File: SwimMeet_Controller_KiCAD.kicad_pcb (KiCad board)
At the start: 2 copper layers, 152.4 x 76.2 mm, 38 parts, among them SW1 LEFT, SW10 RIGHT, SW11 UP, SW12 DOWN, SW13 ACCEPT, SW2 NEXT_HEAT, SW3 PREV_EVENT, SW4 NEXT_EVENT, SW5 PREV_HEAT, SW6 GET_TIMES, SW7 SCORE_EVENT, SW8 CLOSE, SW9 ENTER, U1 Digispark_USB-A_16.5MHz, U2 MCP23017-E_SO

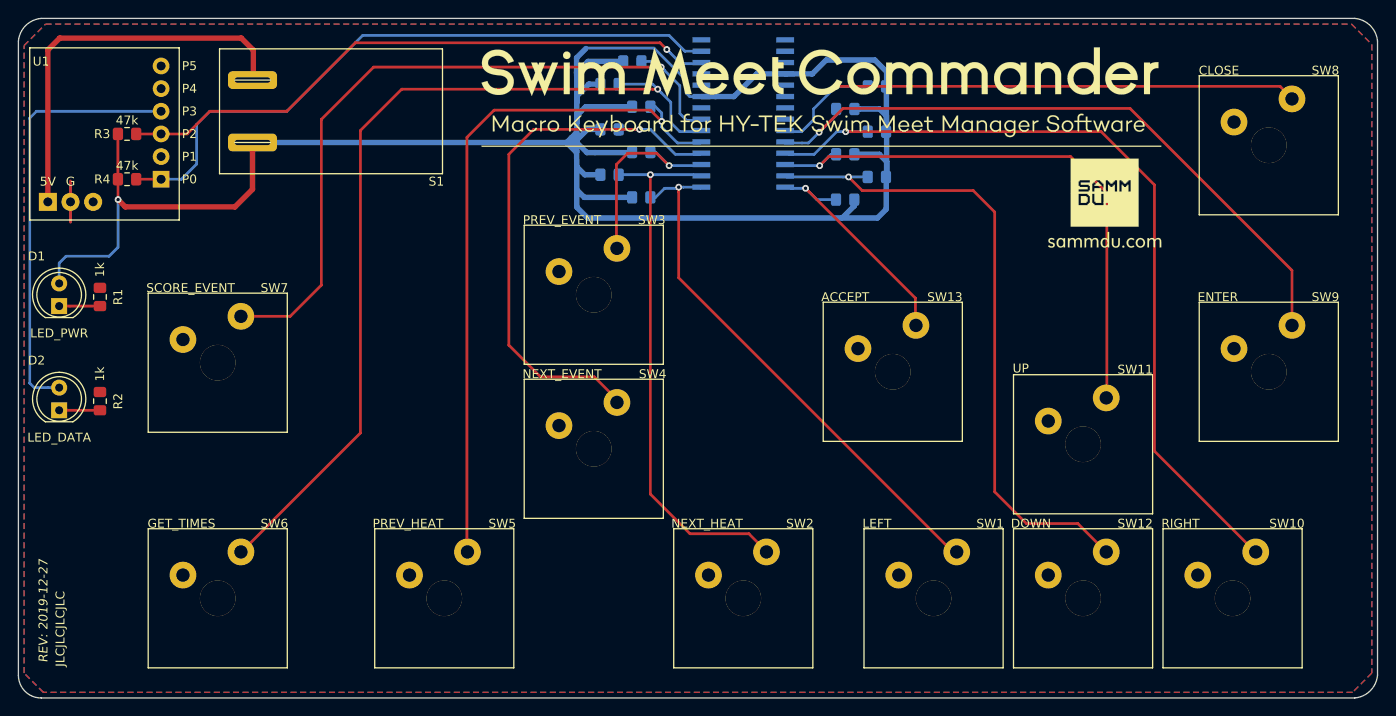
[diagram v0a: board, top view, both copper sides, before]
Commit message: used proper power symbols in schem; made schem compatible with larger grid size; added net names; tidy'ed up PCB more
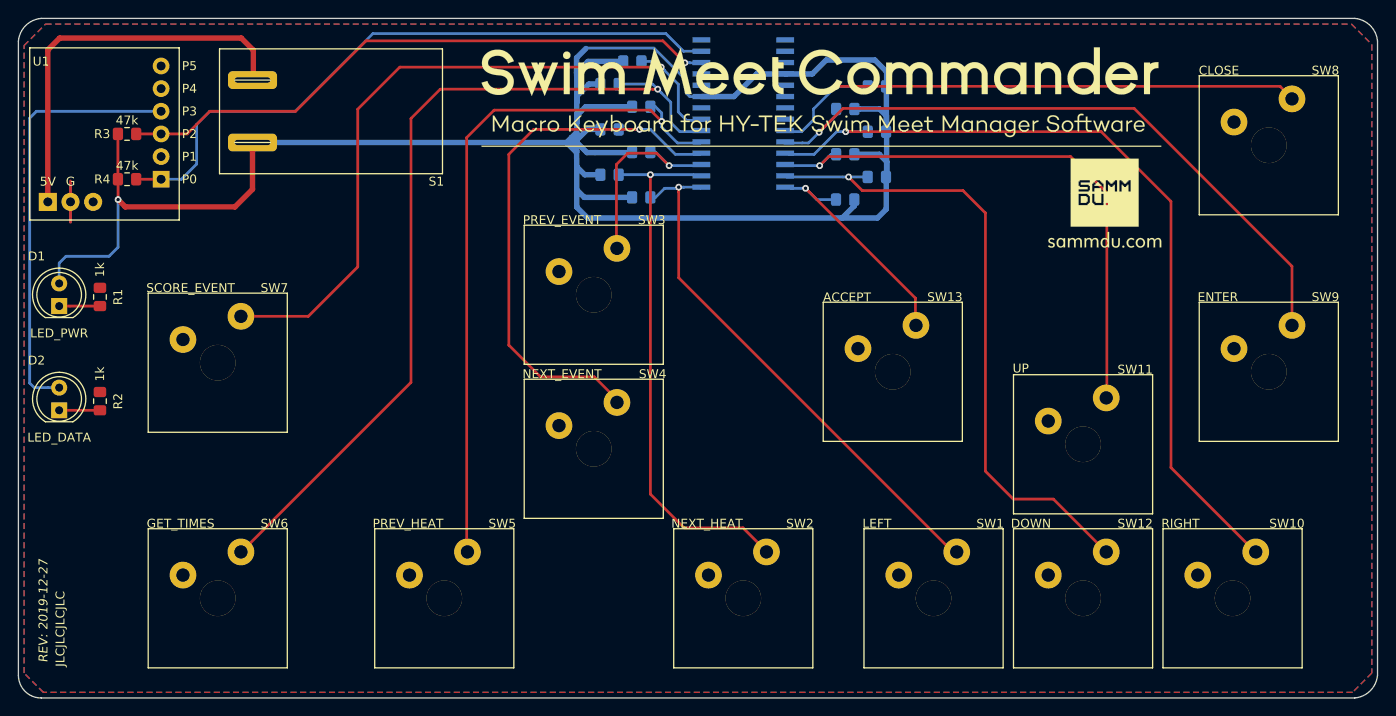
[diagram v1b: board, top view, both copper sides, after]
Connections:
- net 5V renamed +5V
- net Net-(D2-Pad2) renamed /SIG_DATA
- net Net-(S1-Pad2) renamed /VREG
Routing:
- net Net-(R10-Pad2): track 101.2 -> 98.6 mm
- net Net-(R16-Pad2): track 73.8 -> 72.4 mm
- net Net-(R11-Pad2): track 81.3 -> 80.8 mm

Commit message: implemented polygons for 5V+ net
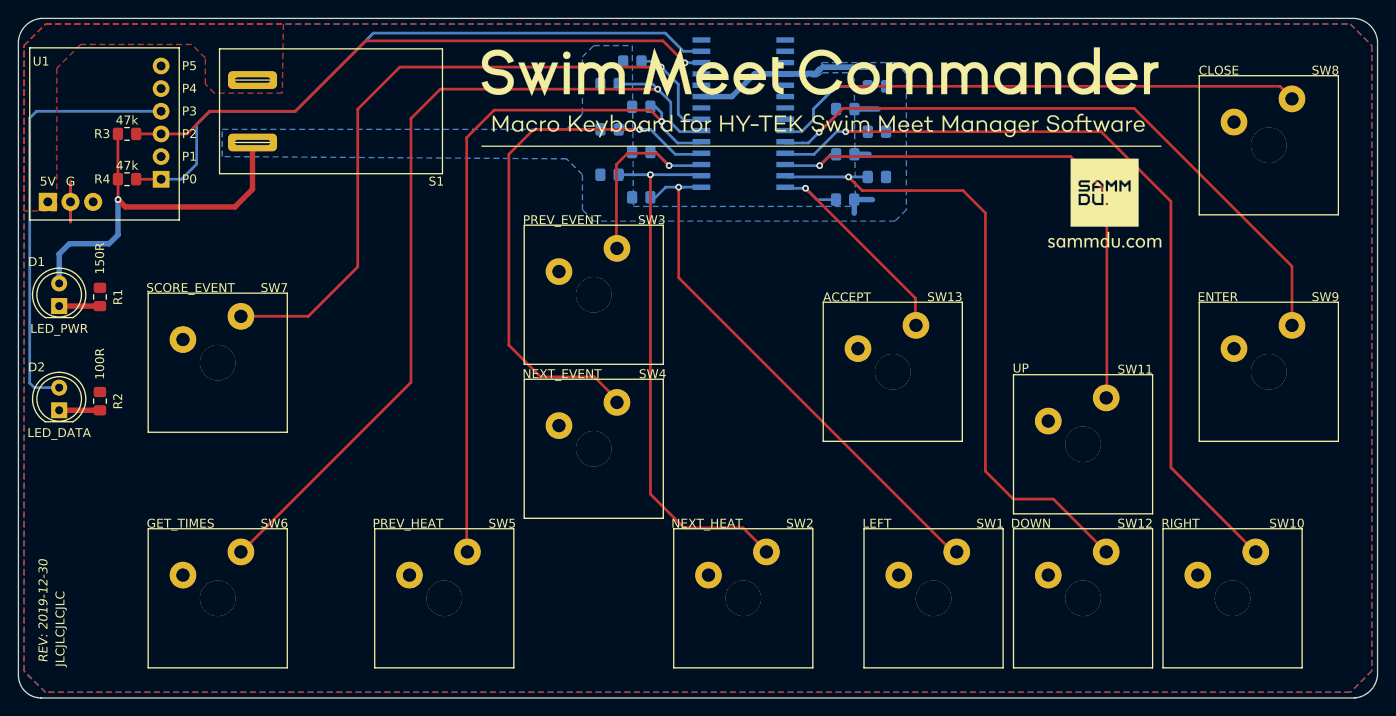
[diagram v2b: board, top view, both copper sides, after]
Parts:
- R1: value 1k -> 150R
- R2: value 1k -> 100R
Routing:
- net +5V: track 246.8 -> 74.9 mm
- net /VREG: track 44.5 -> 0.00 mm
- added copper zone on B.Cu, net +5V
- added copper zone on F.Cu, net /VREG
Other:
- net class Default: clearance 0.2032 -> 0.3048; trace_width 0.3048 -> 0.6096; via_dia 0.762 -> 1.016; via_drill 0.381 -> 0.508
- rule trace_clearance: 0.2032 -> 0.3048
- rule trace_min: 0.2032 -> 0.254
- board text added: "REV: 2019-12-30"
- board text removed: "REV: 2019-12-27"

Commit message: improved power LED connection; updated front silk screen; updated titleblock
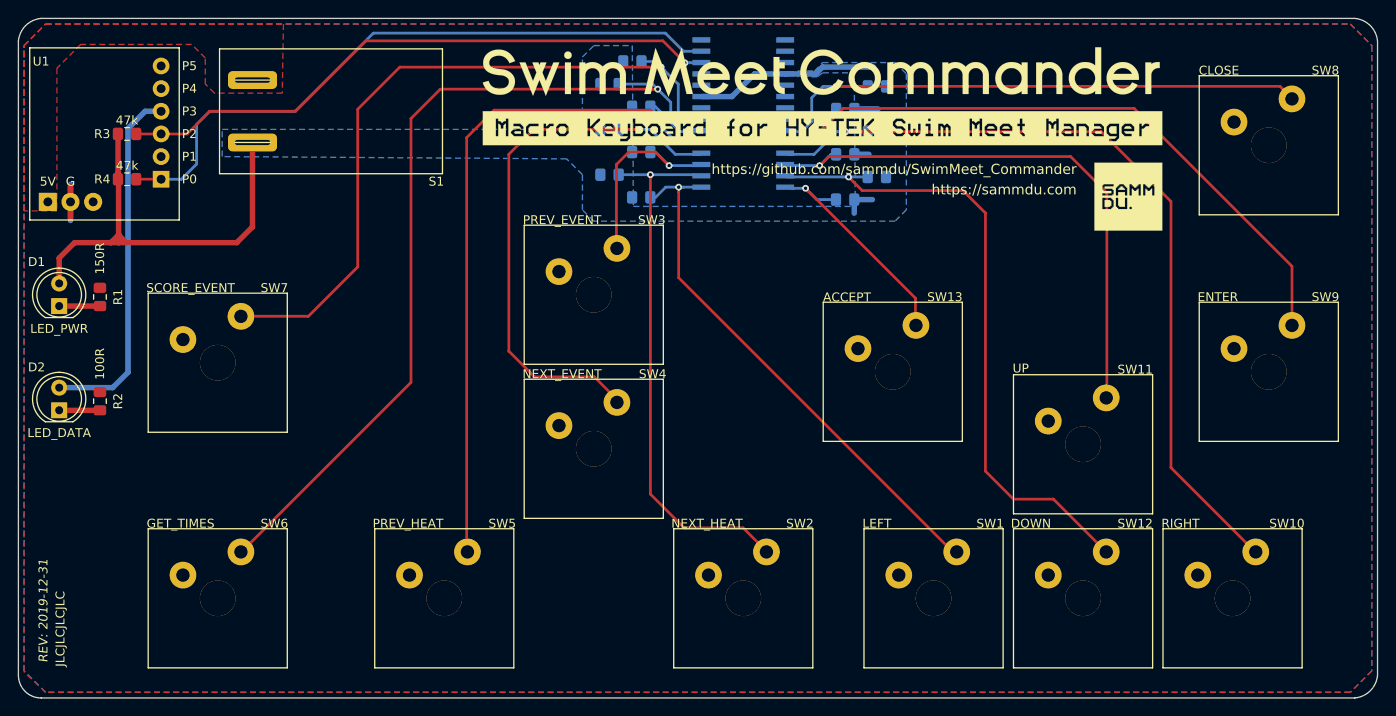
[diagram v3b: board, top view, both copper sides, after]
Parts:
- moved REF** 1.46 mm to (128.4, 26.4)
- moved G*** 0.97 mm to (102.9, 26.2)
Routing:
- net /SIG_DATA: track 48.7 -> 40.3 mm
- net +5V: track 74.9 -> 81.5 mm, vias 1 -> 0
- net GND: track 8.83 -> 7.72 mm
- net Net-(R12-Pad2): track 63.9 -> 64.7 mm
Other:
- board text added: "REV: 2019-12-31"
- board text added: "https://github.com/sammdu/SwimMeet_Commander"
- board text added: "https://sammdu.com"
- board text removed: "REV: 2019-12-30"

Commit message: adjusted resistor values, updated F.Silk graphic, updated toggle switch footprint
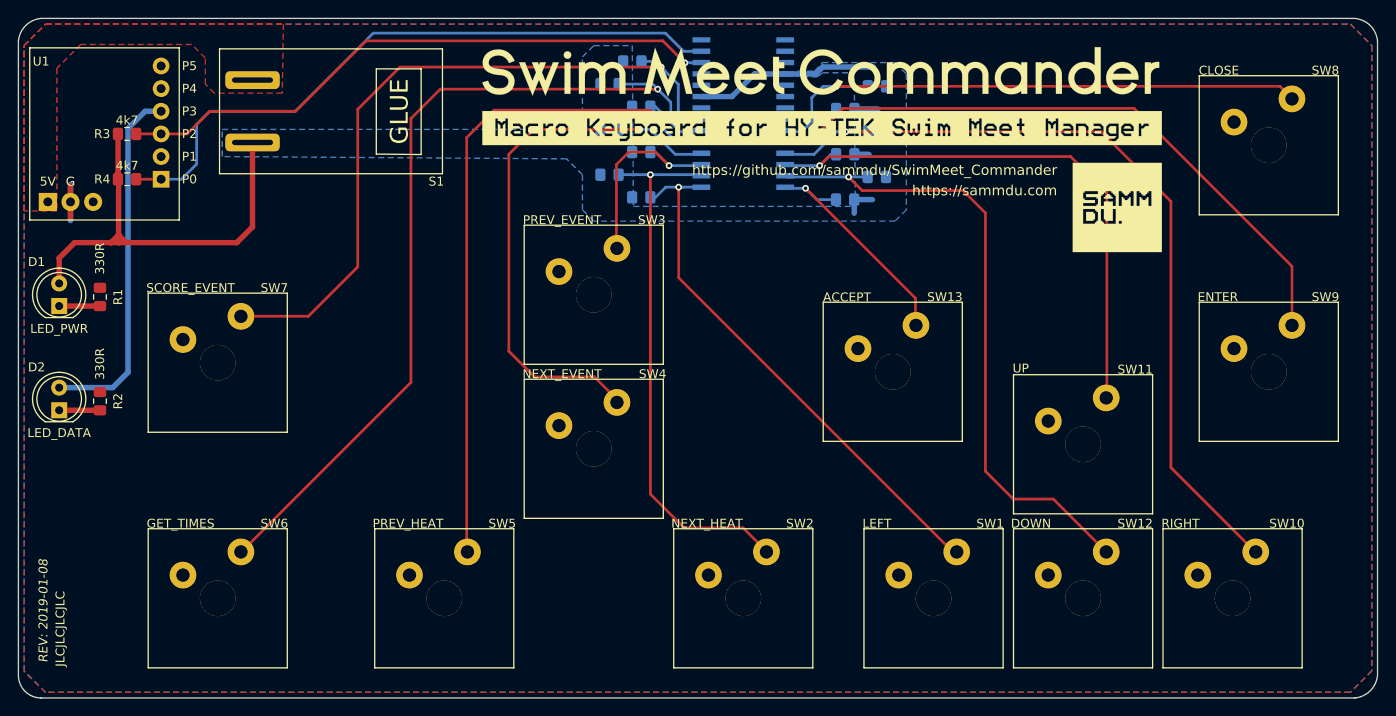
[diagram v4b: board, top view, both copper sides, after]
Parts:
- R1: value 150R -> 330R
- R10, R11, R12, R13, R14, R15, R16, R17, R5, R6, R7, R8, R9: value 1k -> 10k
- R2: value 100R -> 330R
- R3, R4: value 47k -> 4k7
- moved G*** 0.76 mm to (102.8, 27.0)
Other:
- board text added: "REV: 2019-01-08"
- board text removed: "REV: 2019-12-31"

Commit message: MAJOR REVISION 2020-01-12
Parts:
- added ?: , , F.Cu at (18.8, 36.3)
- added R5: 4k7, Resistor_SMD:R_0805_2012Metric_Pad1.15x1.40mm_HandSolder, F.Cu at (24.9, 30.7)
- added S2: DEBUG, spk_Switches:SWITCH_SPST_SMD_A, F.Cu at (16.9, 65.8)
- R4: value 4k7 -> 10k
- moved R4 2.54 mm to (24.9, 28.2)
- renumbered R9 to R10, R10 to R11, R11 to R12, R12 to R13, R13 to R14, R14 to R15, R15 to R16, R16 to R17, R17 to R18, R5 to R6, R6 to R7, R7 to R8, R8 to R9
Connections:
- R4 pad 1: SDA -> /SIG_DEBUG
- R4 pad 2: +5V -> GND
- U1 pad 1: Net-(U1-Pad1) -> /SIG_DEBUG
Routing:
- net +5V: track 81.5 -> 159.4 mm, vias 0 -> 1
- net /SIG_DEBUG: track 0.00 -> 57.2 mm, vias 0 -> 2
- net GND: track 7.72 -> 9.40 mm, vias 0 -> 1
- net /SIG_DATA: track 40.3 -> 40.8 mm
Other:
- outline, holes or cut-outs redrawn
- board text added: "NORMAL_OPS"
- board text added: "NOT endorsed or sponsored by HY-TEK Sports Software®, Active Network, LLC., or any of their affiliates."
- board text added: "Programmed with ARDUINO®"
- board text added: "REV: 2020-01-12"
- board text removed: "REV: 2019-01-08"
